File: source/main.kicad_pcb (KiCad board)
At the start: 4 copper layers, 38 x 75 mm, 62 parts, among them J1 pf_533984002, J2 B4B_ZR_SM4_TF, J3 QWIIC, Q1 MOSFET, SW1 _Switch, SW2 _Switch, U1 SCD40, U2 ME6211C33M5G_N, U3 pf_74AHCT2G125, U4 BH1750FVI_TR, U5 ESP32_C3_MINI_1_VIND, U6 TXS0102DCUR, U7 HLK_LD2410B_P, U8 USBLC6_2P6, x1 USB_Type_C_Receptacle_14_pin_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

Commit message: Port layout (wip)
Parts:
- removed C11, C19, C21: 100nF, lcsc:C0402
- removed C20: 1µF, lcsc:C0402
- removed R15, R16: 5.1kΩ, lcsc:R0402
- removed R17: 1MΩ, lcsc:R0402
- removed R3: 1kΩ, lcsc:R0402
- removed SW1, SW2: _Switch, lcsc:KEY-SMD_4P-L4.2-W3.2-P2.20-LS4.6
- added J4: B4B_ZR_SM4_TF, lcsc:CONN-SMD_ZH1.5-4AB, F.Cu at (-34.4, 43.2)
- C1, C13, C14, C16, C5: value 100nF -> 100nF 16V X7R
- C10, C6, C7, C8, C9: value 100nF -> 100nF 16V X7R; moved to F.Cu
- C12: value 1µF -> 100nF 16V X7R; moved to F.Cu
- C15, C3, C4: value 1µF -> 100nF 16V X7R
- C17: value 10µF -> 1µF 25V X5R; footprint lcsc:C0805 -> lcsc:C0402
- C18: value 100nF -> 100nF 1kV X7R; footprint lcsc:C0402 -> lcsc:C2220
- C2: value 4.7µF -> 100nF 16V X7R
- D1: footprint lcsc:LED0805-RD_RED -> lcsc:LED0805-R-RD
- LED1, LED2, LED3, LED4, LED5: moved to F.Cu
- R1, R2, R6, R7, R8, R9: value 10kΩ -> 100Ω
- R10: value 10kΩ -> 100kΩ
- R11: value 100kΩ -> 100Ω
- R12: value 1kΩ -> 5.1kΩ
- R13: value 390Ω -> 5.1kΩ
- R14: value 390Ω -> 1MΩ
- R4, R5: value 10kΩ -> 100Ω; moved to F.Cu
- U3: value pf_74AHCT2G125 -> TXS0102DCUR; footprint lcsc:SC-74A-5_L2.9-W1.6-P0.95-LS2.8-BR -> lcsc:VSON8_L2.0-W2.3-P0.50-LS3.1-BL
- U4: value BH1750FVI_TR -> ESP32_C3_MINI_1; footprint lcsc:WSOF-6_L2.6-W1.6-P0.50-TL-EP -> lcsc:WIFIM-SMD_ESP32-C3-MINI-MINI-1U; moved to F.Cu
- U5: value ESP32_C3_MINI_1_VIND -> TXS0102DCUR; footprint lcsc:WIFIM-SMD_ESP32-C3-MINI-MINI-1U -> lcsc:VSON8_L2.0-W2.3-P0.50-LS3.1-BL
- U6: value TXS0102DCUR -> USBLC6_2P6; footprint lcsc:VSON8_L2.0-W2.3-P0.50-LS3.1-BL -> lcsc:SOT-666-6_L1.6-W1.2-P0.50-LS1.6-BL
- U7: value HLK_LD2410B_P -> BH1750FVI_TR; footprint lcsc:SENSORM-TH_HLK-LD2410B-P -> lcsc:WSOF-6_L2.6-W1.6-P0.50-TL-EP; moved to F.Cu
- U8: value USBLC6_2P6 -> HLK_LD2410B_P; footprint lcsc:SOT-666-6_L1.6-W1.2-P0.50-LS1.6-BL -> lcsc:SENSORM-TH_HLK-LD2410B-P
- moved C18 70.5 mm to (-5.50, 73.0)
- moved LED5 69.5 mm to (-55.7, 52.7)
- moved R13 66.9 mm to (0.50, 68.5), turned to 90 degrees
- moved R14 65.6 mm to (1.50, 68.5), turned to 90 degrees
- moved LED4 63.9 mm to (-55.7, 48.4)
- moved U6 62.2 mm to (-5.00, 64.5), turned to 0 degrees
- moved C3 60.2 mm to (-41.0, 24.9), turned to 0 degrees
- moved C13 59.7 mm to (-34.0, 20.6), turned to 0 degrees
- moved LED3 59.5 mm to (-55.7, 44.1)
- moved U7 56.9 mm to (0.00, 7.00), turned to 180 degrees
- moved LED2 56.7 mm to (-55.7, 39.8)
- moved LED1 55.7 mm to (-55.7, 35.5)
- moved U3 55.5 mm to (-50.8, 53.0), turned to 0 degrees
- moved C4 54.5 mm to (-41.0, 27.0), turned to 0 degrees
- moved R8 54.2 mm to (-27.8, 24.9), turned to 0 degrees
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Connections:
- C12 pad 1: C12-1-R3-1-U4-5 -> 3V3
- C13 pad 1: C13-1-R8-2-SW1-1-SW1-2 -> 3V3
- C14 pad 1: C14-1-R9-2-SW2-1-SW2-2 -> 3V3
- C15 pad 1: C15-1-R10-1-R9-1-U5-8 -> VBUS
- C16 pad 1: 3V3 -> VBUS
- C17 pad 1: 3V3 -> C17-1
- C17 pad 2: GND -> C17-2
- C18 pad 1: 3V3 -> C18-1-R14-1-x1-0
- C2 pad 1: 3V3 -> VBUS
- C3 pad 1: VBUS -> 3V3
- C4 pad 1: 3V3 -> VBUS
- C5 pad 1: C5-1-U3-5 -> VBUS
- C5 pad 2: C5-2-U3-1-U3-3 -> GND
- D1 pad 2: D1-2-R12-2 -> D1-2-R11-1
- J2 pad 1: J2-1-R14-2 -> J2-1
- J2 pad 2: J2-2-R13-2 -> J2-2
- J2 pad 3: VBUS -> J2-3
- J2 pad 4: GND -> J2-4
- LED1 pad 1: LED1-1-U3-4 -> GND
- LED1 pad 2: GND -> LED1-2-U3-8
- LED1 pad 4: LED1-4-LED2-1 -> LED1-4-LED2-2
- LED2 pad 1: LED1-4-LED2-1 -> GND
- LED2 pad 2: GND -> LED1-4-LED2-2
- LED2 pad 4: LED2-4-LED3-1 -> LED2-4-LED3-2
- LED3 pad 1: LED2-4-LED3-1 -> GND
- LED3 pad 2: GND -> LED2-4-LED3-2
- LED3 pad 4: LED3-4-LED4-1 -> LED3-4-LED4-2
- LED4 pad 1: LED3-4-LED4-1 -> GND
- LED4 pad 2: GND -> LED3-4-LED4-2
- LED4 pad 4: LED4-4-LED5-1 -> LED4-4-LED5-2
- LED5 pad 1: LED4-4-LED5-1 -> GND
- LED5 pad 2: GND -> LED4-4-LED5-2
- Q1 pad 1: Q1-1-R11-1-U5-21 -> Q1-1-R9-1-U4-21
- R1 pad 1: SDA -> SCL
- R10 pad 1: C15-1-R10-1-R9-1-U5-8 -> R10-1
- R10 pad 2: 3V3 -> R10-2
- R11 pad 1: Q1-1-R11-1-U5-21 -> D1-2-R11-1
- R11 pad 2: GND -> R11-2
- R12 pad 1: R12-1 -> R12-1-x1-12
- R12 pad 2: D1-2-R12-2 -> GND
- R13 pad 1: U1_RX_BHV -> R13-1-x1-5
- R13 pad 2: J2-2-R13-2 -> GND
- R14 pad 1: U1_TX_BHV -> C18-1-R14-1-x1-0
- R14 pad 2: J2-1-R14-2 -> GND
- R2 pad 1: SCL -> SDA
- R4 pad 1: SDA -> SCL
- R5 pad 1: SCL -> SDA
- R6 pad 1: R6-1-U5-22 -> R6-1-U4-8
- R6 pad 2: 3V3 -> R6-2
- R7 pad 1: R7-1-U5-5 -> R7-1-U4-5
- R7 pad 2: 3V3 -> R7-2
- R8 pad 1: R8-1-U5-23 -> R8-1-U4-22
- R8 pad 2: C13-1-R8-2-SW1-1-SW1-2 -> R8-2
- R9 pad 1: C15-1-R10-1-R9-1-U5-8 -> Q1-1-R9-1-U4-21
- R9 pad 2: C14-1-R9-2-SW2-1-SW2-2 -> R9-2
- U3 pad 1: C5-2-U3-1-U3-3 -> U3-1
- U3 pad 2: U3-2 -> GND
- U3 pad 3: C5-2-U3-1-U3-3 -> VBUS
- U3 pad 4: LED1-1-U3-4 -> U3-4
- U3 pad 5: C5-1-U3-5 -> U3-5
- U4 pad 1: 3V3 -> GND
- U4 pad 2: U4-2 -> GND
- U4 pad 3: GND -> 3V3
- U4 pad 4: SDA -> U4-4
- U4 pad 5: C12-1-R3-1-U4-5 -> R7-1-U4-5
- U4 pad 6: SCL -> U4-6
- U5 pad 1: GND -> U5-1
- U5 pad 5: R7-1-U5-5 -> U5-5
- U5 pad 6: U5-6 -> 3V3
- U5 pad 7: U5-7 -> VBUS
- U5 pad 8: C15-1-R10-1-R9-1-U5-8 -> U5-8
- U6 pad 1: U1_RX_BHV -> USB_DP
- U6 pad 3: 3V3 -> USB_DN
- U6 pad 4: U1_RX -> USB_DN
- U6 pad 5: U1_TX -> VBUS
- U6 pad 6: GND -> USB_DP
- U7 pad 1: U5-20-U7-1 -> 3V3
- U7 pad 2: U0_TX -> U7-2
- U7 pad 3: U0_RX -> GND
- U7 pad 4: GND -> SDA
- U7 pad 5: VBUS -> U7-5
- U8 pad 1: USB_DP -> U4-20-U8-1
- U8 pad 2: GND -> DSF_MCU_UART0_TX
- U8 pad 3: USB_DN -> DSF_MCU_UART0_RX
- U8 pad 4: USB_DN -> GND
- x1 pad 0: C21-1-R17-1-x1-0 -> C18-1-R14-1-x1-0
- x1 pad 12: R15-1-x1-12 -> R12-1-x1-12
- x1 pad 5: R16-1-x1-5 -> R13-1-x1-5
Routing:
- net (no net): track 0.00 -> 70.6 mm, vias 0 -> 2
- net LED1-1-U3-4: track 12.0 -> 0.00 mm, vias 1 -> 0
- net LED4-4-LED5-1: track 8.46 -> 0.00 mm
- net LED2-4-LED3-1: track 8.46 -> 0.00 mm
- net LED1-4-LED2-1: track 8.46 -> 0.00 mm
- net LED3-4-LED4-1: track 8.46 -> 0.00 mm
- net C21-1-R17-1-x1-0: track 8.03 -> 0.00 mm
- net C17-2: track 0.00 -> 7.58 mm
- net C14-1-R9-2-SW2-1-SW2-2: track 7.58 -> 0.00 mm
- net C13-1-R8-2-SW1-1-SW1-2: track 7.58 -> 0.00 mm
- net R16-1-x1-5: track 6.74 -> 0.00 mm
- net R15-1-x1-12: track 5.63 -> 0.00 mm
- net R12-1-x1-12: track 0.00 -> 5.63 mm
- net R6-1-U4-8: track 0.00 -> 4.67 mm
- net C15-1-R10-1-R9-1-U5-8: track 4.67 -> 0.00 mm
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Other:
- outline, holes or cut-outs redrawn

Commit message: Various fixes and changes
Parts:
- removed R11, R6: 100Ω, lcsc:R0402
- removed R12, R13: 5.1kΩ, lcsc:R0402
- removed R14: 1MΩ, lcsc:R0402
- removed x1: USB_Type_C_Receptacle_14_pin_Vertical, lcsc:USB-C-TH_TYPE-C-USB-14P
- added C11: 1µF 25V X5R, lcsc:C0402, B.Cu at (1.50, 32.3)
- added C19: 1µF 25V X5R, lcsc:C0402, F.Cu at (-6.00, 61.5)
- added C20: 100nF 16V X7R, lcsc:C0402, F.Cu at (-2.50, 68.5)
- added D2: LED, lcsc:LED0805-R-RD, F.Cu at (8.00, 30.0)
- added F1: Fuse, lcsc:F0603, F.Cu at (15.0, 7.50)
- added F2: Fuse, lcsc:F0402, F.Cu at (2.75, 68.5)
- added R3: 100Ω, lcsc:R0402, B.Cu at (3.00, 6.00)
- added S1: Button, lcsc:KEY-SMD_4P-L4.2-W3.2-P2.20-LS4.6, F.Cu at (13.5, 61.5)
- added S2: Button, lcsc:KEY-SMD_4P-L4.2-W3.2-P2.20-LS4.6, F.Cu at (-13.5, 61.5)
- added U9: USB2_0_ESD_Protection, lcsc:SOT-666-6_L1.6-W1.2-P0.50-LS1.6-BL, F.Cu at (-8.00, 61.5)
- C1, C14, C15, C16, C2, C3, C4, C5, C6, C7: value 100nF 16V X7R -> 1µF 25V X5R
- C10, C12, C8, C9: value 100nF 16V X7R -> 1µF 25V X5R; moved to B.Cu
- C13, LED1, LED2, LED3, LED4, LED5, R4, U8: moved to B.Cu
- C18: value 100nF 1kV X7R -> 1µF 25V X5R; footprint lcsc:C2220 -> lcsc:C0402
- D1: value LED -> 1.1V; footprint lcsc:LED0805-R-RD -> lcsc:SOD-123F_L2.8-W1.8-LS3.7-RD
- H1, H2, H3: footprint MountingHole:MountingHole_2.1mm -> MountingHole:MountingHole_2mm
- J4: value B4B_ZR_SM4_TF -> USB_Type_C_Receptacle_14_pin_Vertical; footprint lcsc:CONN-SMD_ZH1.5-4AB -> lcsc:USB-C-TH_TYPE-C-USB-14P
- R10: value 100kΩ -> 1MΩ
- R8, R9: value 100Ω -> 5.1kΩ
- U3: value TXS0102DCUR -> ME6211C33M5G_N; footprint lcsc:VSON8_L2.0-W2.3-P0.50-LS3.1-BL -> lcsc:SOT-23-5_L3.0-W1.7-P0.95-LS2.8-BL
- U4: value ESP32_C3_MINI_1 -> TXS0102DCUR; footprint lcsc:WIFIM-SMD_ESP32-C3-MINI-MINI-1U -> lcsc:VSON8_L2.0-W2.3-P0.50-LS3.1-BL
- U5: value TXS0102DCUR -> BH1750FVI_TR; footprint lcsc:VSON8_L2.0-W2.3-P0.50-LS3.1-BL -> lcsc:WSOF-6_L2.6-W1.6-P0.50-TL-EP; moved to B.Cu
- U6: value USBLC6_2P6 -> ESP32_C3_MINI_1; footprint lcsc:SOT-666-6_L1.6-W1.2-P0.50-LS1.6-BL -> lcsc:WIFIM-SMD_ESP32-C3-MINI-MINI-1U
- U7: value BH1750FVI_TR -> TXS0102DCUR; footprint lcsc:WSOF-6_L2.6-W1.6-P0.50-TL-EP -> lcsc:VSON8_L2.0-W2.3-P0.50-LS3.1-BL
- moved C18 70.8 mm to (-3.00, 2.20)
- moved C17 62.6 mm to (3.25, 2.80), turned to -90 degrees
- moved LED1 60.8 mm to (0.00, 11.0), turned to 180 degrees
- moved LED2 60.1 mm to (0.00, 17.1), turned to 180 degrees
- moved LED3 59.5 mm to (0.00, 23.2), turned to 180 degrees
- moved LED4 58.9 mm to (0.00, 29.3), turned to 180 degrees
- moved LED5 58.3 mm to (0.00, 35.4), turned to 180 degrees
- moved C5 57.1 mm to (3.85, 64.5), turned to -90 degrees
- moved C4 56.5 mm to (5.60, 59.0), turned to 180 degrees
- moved U3 56.4 mm to (5.00, 61.5), turned to 90 degrees
- moved C3 55.5 mm to (-2.15, 64.5), turned to -90 degrees
- moved C2 54.5 mm to (-0.40, 59.0), turned to 180 degrees
- moved U6 51.8 mm to (-11.0, 13.0), turned to 90 degrees
- moved R8 51.0 mm to (-1.25, 68.5), turned to 90 degrees
- moved R9 49.9 mm to (0.00, 68.5), turned to 90 degrees
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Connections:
- net U7-5 renamed DSF_MCU_UART1_RX
- C1 pad 1: 3V3 -> 3V3_PERIPHERAL
- C10 pad 1: VBUS -> 5V
- C12 pad 1: 3V3 -> 5V
- C13 pad 1: 3V3 -> 3V3_PERIPHERAL
- C14 pad 1: 3V3 -> 3V3_MCU
- C15 pad 1: VBUS -> MCU_GPIO0
- C16 pad 1: VBUS -> MCU_GPIO1
- C17 pad 1: C17-1 -> 3V3_PERIPHERAL
- C17 pad 2: C17-2 -> GND
- C18 pad 1: C18-1-R14-1-x1-0 -> 5V
- C2 pad 1: VBUS -> 5V
- C3 pad 1: 3V3 -> 3V3_MCU
- C4 pad 1: VBUS -> 5V
- C5 pad 1: VBUS -> 3V3_PERIPHERAL
- C6 pad 1: VBUS -> 3V3_PERIPHERAL
- C7 pad 1: VBUS -> 5V
- C8 pad 1: VBUS -> 5V
- C9 pad 1: VBUS -> 5V
- D1 pad 1: VBUS -> D1-1-J1-1-Q1-2-R7-2
- D1 pad 2: D1-2-R11-1 -> 5V
- J1 pad 1: J1-1-Q1-2 -> D1-1-J1-1-Q1-2-R7-2
- J1 pad 2: VBUS -> 5V
- J2 pad 1: J2-1 -> USF_PM_SENSOR_LEVEL_SHIFTER_RX
- J2 pad 2: J2-2 -> USF_PM_SENSOR_LEVEL_SHIFTER_TX
- J2 pad 3: J2-3 -> 5V
- J2 pad 4: J2-4 -> GND
- J3 pad 2: 3V3 -> F1-1-J3-2
- J4 pad 1: DFS_MCU_UART1_RX -> GND
- J4 pad 2: DFS_MCU_UART1_TX -> VBUS
- J4 pad 3: J4-3 -> USB_DN
- J4 pad 4: J4-4 -> USB_DP
- J4 pad 5: J4-5 -> J4-5-R9-1
- J4 pad 6: J4-6 -> VBUS
- LED1 pad 2: LED1-2-U3-8 -> LED1-2-U4-8
- LED1 pad 3: VBUS -> 5V
- LED2 pad 3: VBUS -> 5V
- LED3 pad 3: VBUS -> 5V
- LED4 pad 3: VBUS -> 5V
- LED5 pad 3: VBUS -> 5V
- Q1 pad 1: Q1-1-R9-1-U4-21 -> MCU_GPIO7
- Q1 pad 2: J1-1-Q1-2 -> D1-1-J1-1-Q1-2-R7-2
- R1 pad 2: 3V3 -> 3V3_PERIPHERAL
- R10 pad 1: R10-1 -> C20-1-J4-0-R10-1
- R10 pad 2: R10-2 -> GND
- R2 pad 2: 3V3 -> 3V3_PERIPHERAL
- R4 pad 1: SCL -> SDA
- R4 pad 2: 3V3 -> 3V3_PERIPHERAL
- R5 pad 1: SDA -> MCU_GPIO7
- R5 pad 2: 3V3 -> GND
- R7 pad 1: R7-1-U4-5 -> D2-2-R7-1
- R7 pad 2: R7-2 -> D1-1-J1-1-Q1-2-R7-2
- R8 pad 1: R8-1-U4-22 -> J4-12-R8-1
- R8 pad 2: R8-2 -> GND
- R9 pad 1: Q1-1-R9-1-U4-21 -> J4-5-R9-1
- R9 pad 2: R9-2 -> GND
- U1 pad 19: 3V3 -> 3V3_PERIPHERAL
- U1 pad 7: 3V3 -> 3V3_PERIPHERAL
- U2 pad 1: VBUS -> 5V
- U2 pad 3: VBUS -> 5V
- U2 pad 5: 3V3 -> 3V3_MCU
- U3 pad 1: U3-1 -> 5V
- U3 pad 3: VBUS -> 5V
- U3 pad 5: U3-5 -> 3V3_PERIPHERAL
- U4 pad 1: GND -> U4-1
- U4 pad 3: 3V3 -> 3V3_PERIPHERAL
- U4 pad 5: R7-1-U4-5 -> MCU_GPIO5
- U4 pad 6: U4-6 -> 3V3_PERIPHERAL
- U4 pad 7: U4-7 -> 5V
- U4 pad 8: R6-1-U4-8 -> LED1-2-U4-8
- U5 pad 1: U5-1 -> 3V3_PERIPHERAL
- U5 pad 2: GND -> U5-2
- U5 pad 3: 3V3 -> GND
- U5 pad 4: U5-4 -> SDA
- U5 pad 6: 3V3 -> SCL
- U5 pad 7: VBUS -> U5-7
- U6 pad 1: USB_DP -> GND
- U6 pad 3: USB_DN -> 3V3_MCU
- U6 pad 4: USB_DN -> U6-4
- U6 pad 5: VBUS -> MCU_GPIO2
- U6 pad 6: USB_DP -> MCU_GPIO3
- U7 pad 1: 3V3 -> USF_PM_SENSOR_LEVEL_SHIFTER_TX
- U7 pad 2: U7-2 -> GND
- U7 pad 3: GND -> 3V3_PERIPHERAL
- U7 pad 4: SDA -> DSF_MCU_UART1_TX
- U7 pad 6: SCL -> 3V3_PERIPHERAL
- U7 pad 7: U7-7 -> 5V
- U8 pad 1: U4-20-U8-1 -> MCU_GPIO6
- U8 pad 5: VBUS -> 5V
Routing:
- net (no net): track 70.6 -> 0.00 mm, vias 2 -> 0
- net VBUS: track 56.0 -> 17.6 mm, vias 5 -> 1
- net 3V3: track 32.9 -> 0.00 mm, vias 1 -> 0
- net USB_DP: track 72.7 -> 54.6 mm, vias 3 -> 1
- net USB_DN: track 72.7 -> 54.7 mm, vias 3 -> 1
- net SDA: track 0.00 -> 17.4 mm, vias 0 -> 2
- net SCL: track 0.00 -> 16.1 mm, vias 0 -> 2
- net 5V: track 0.00 -> 12.9 mm, vias 0 -> 4
- net 3V3_PERIPHERAL: track 0.00 -> 12.8 mm
- net D1-1-J1-1-Q1-2-R7-2: track 0.00 -> 12.8 mm
- net F1-1-J3-2: track 0.00 -> 8.05 mm, vias 0 -> 2
- net C17-2: track 7.58 -> 0.00 mm
- net R12-1-x1-12: track 5.63 -> 0.00 mm
- net J4-5-R9-1: track 0.00 -> 5.53 mm
- net C20-1-J4-0-R10-1: track 0.00 -> 5.08 mm
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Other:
- outline, holes or cut-outs redrawn
- board text added: "80082e6"
- board text added: "Vindriktning"

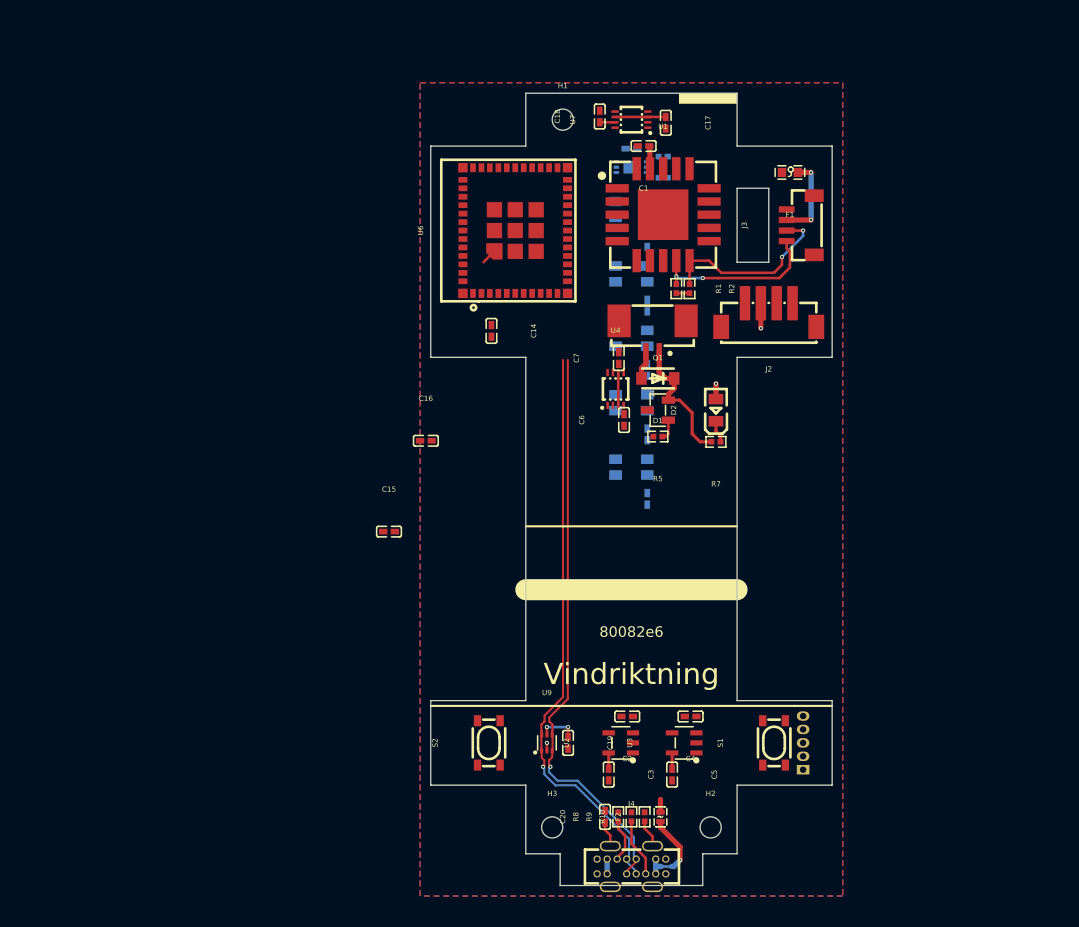
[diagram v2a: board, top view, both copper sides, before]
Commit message: fix power source short
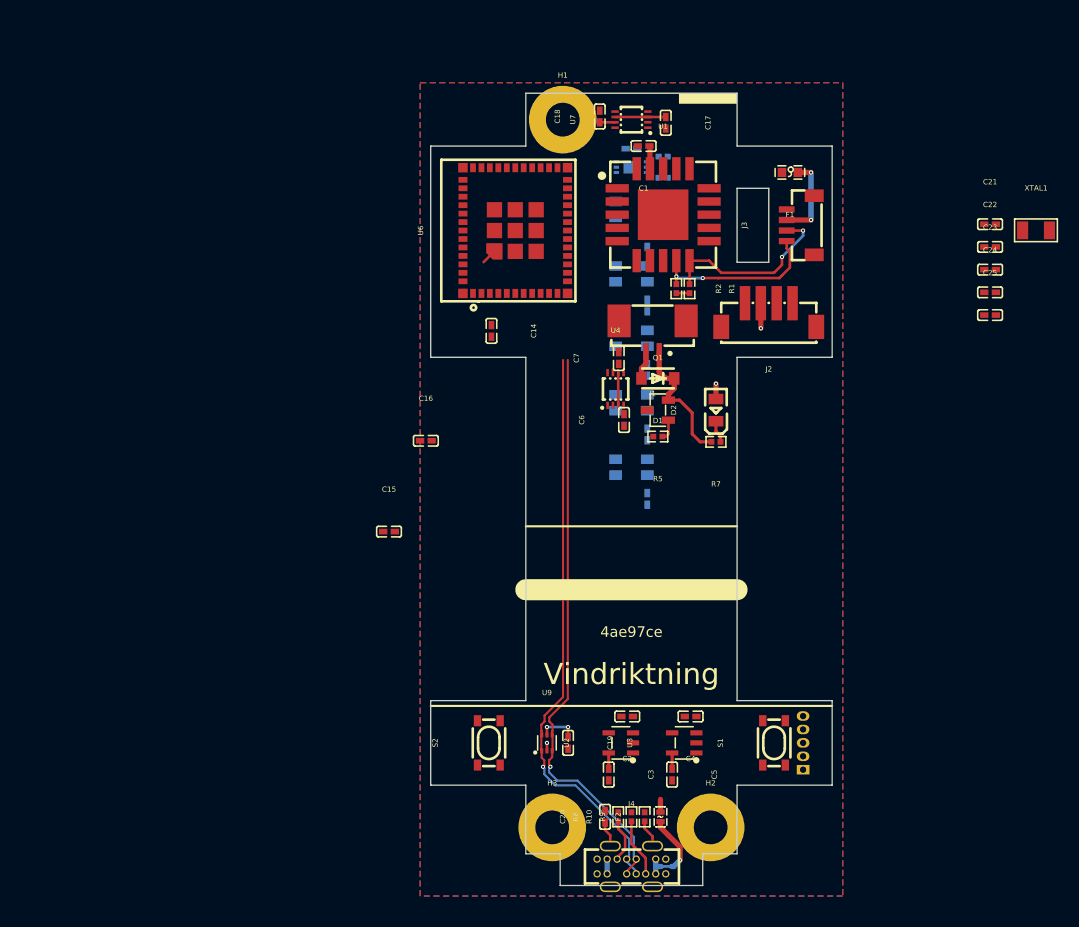
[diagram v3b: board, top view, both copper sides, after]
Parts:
- added C21: 100nF 16V X7R, lcsc:C0402, F.Cu at (34.0, 12.4)
- added C22: 100nF 16V X7R, lcsc:C0402, F.Cu at (34.0, 14.6)
- added C23: 100nF 16V X7R, lcsc:C0402, F.Cu at (34.0, 16.7)
- added C24: 100nF 16V X7R, lcsc:C0402, F.Cu at (34.0, 18.9)
- added C25: 100nF 16V X7R, lcsc:C0402, F.Cu at (34.0, 21.0)
- added XTAL1: Crystal, lcsc:CRYSTAL-SMD_L3.2-W1.5-1, F.Cu at (38.3, 13.0)
- C1, C10, C11, C12, C14, C17, C18, C19, C2, C3, C4, C5, C6, C7, C8, C9: value 1µF 25V X5R -> 100nF 16V X7R
- C15, C16: value 1µF 25V X5R -> 15pF 50V C0G
- D2: value LED -> 2V
- H1, H2, H3: footprint MountingHole:MountingHole_2mm -> MountingHole:MountingHole_3.2mm_M3_Pad
- R7: value 100Ω -> 2.2kΩ
- U2: value ME6211C33M5G_N -> LDO 3.3V ±2% Vin max 4.8V - 5.2V Iq
- U3: value ME6211C33M5G_N -> LDO 3.3V Vin max 4.8V - 5.2V Iq
- moved LED3 12.2 mm to (0.00, 11.0)
- moved LED5 12.2 mm to (0.00, 23.2)
- moved LED2 12.2 mm to (0.00, 29.3)
- moved LED1 6.10 mm to (0.00, 17.1)
- moved LED4 6.10 mm to (0.00, 35.4)
- moved R1 1.25 mm to (5.50, 18.5)
- moved R10 1.25 mm to (0.00, 68.5)
- moved R2 1.25 mm to (4.25, 18.5)
- moved R9 1.25 mm to (1.25, 68.5)
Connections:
- C6 pad 1: 3V3_PERIPHERAL -> 5V
- R1 pad 2: 3V3_PERIPHERAL -> R1-2-R2-2
- R2 pad 2: 3V3_PERIPHERAL -> R1-2-R2-2
- S1 pad 1: S1-1-S1-2 -> S1-1-S1-2-U6-8
- S1 pad 2: S1-1-S1-2 -> S1-1-S1-2-U6-8
- S1 pad 3: S1-3-S1-4 -> GND
- S1 pad 4: S1-3-S1-4 -> GND
- S2 pad 1: S2-1-S2-2 -> MCU_GPIO9
- S2 pad 2: S2-1-S2-2 -> MCU_GPIO9
- S2 pad 3: S2-3-S2-4 -> GND
- S2 pad 4: S2-3-S2-4 -> GND
- U2 pad 3: 5V -> U2-3-U3-3
- U3 pad 3: 5V -> U2-3-U3-3
- U6 pad 8: U6-8 -> S1-1-S1-2-U6-8
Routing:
- net R1-2-R2-2: track 0.00 -> 1.25 mm
- net 3V3_PERIPHERAL: track 12.8 -> 11.6 mm
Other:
- board text added: "4ae97ce"
- board text removed: "80082e6"

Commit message: Fix some layout
- Add named net for fan
- Add part db to gitignore
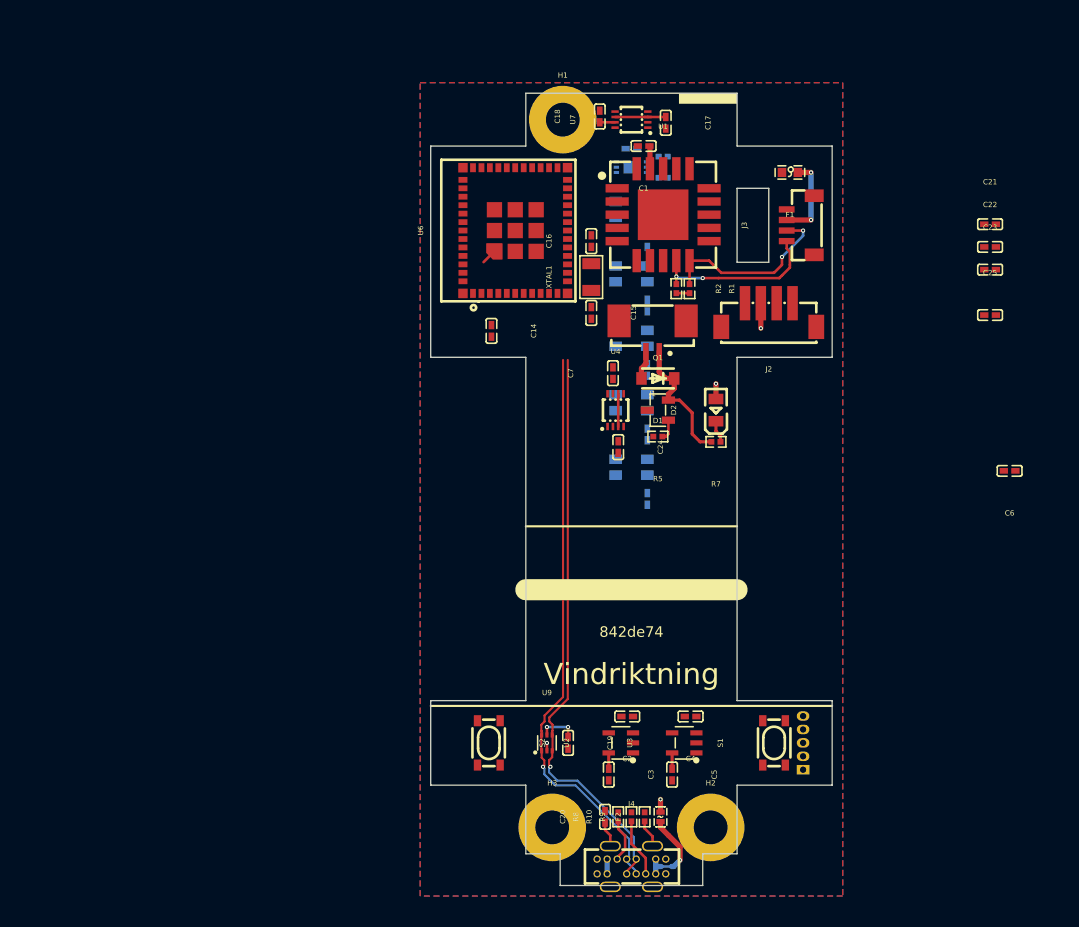
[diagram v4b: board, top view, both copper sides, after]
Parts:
- moved XTAL1 42.3 mm to (-3.80, 17.4), turned to 90 degrees
- moved C24 38.1 mm to (-1.25, 33.5), turned to -90 degrees
- moved C6 36.8 mm to (35.8, 35.8), turned to 180 degrees
- moved C15 28.2 mm to (-3.80, 20.8), turned to -90 degrees
- moved C16 24.5 mm to (-3.80, 14.0), turned to 90 degrees
- moved LED3 18.3 mm to (0.00, 29.3)
- moved LED4 18.3 mm to (0.00, 17.1)
- moved LED5 12.2 mm to (0.00, 35.4)
- moved LED1 6.10 mm to (0.00, 11.0)
- moved LED2 6.10 mm to (0.00, 23.2)
- moved R3 2.00 mm to (3.00, 8.00)
- moved R4 2.00 mm to (3.00, 6.00)
- moved U4 2.00 mm to (-1.50, 30.0)
- moved C7 1.53 mm to (-1.75, 26.5)
- turned S2 to -90 degrees
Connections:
- net D1-1-J1-1-Q1-2-R7-2 renamed FAN_OUT-
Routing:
- net 5V: vias 4 -> 5
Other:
- board text added: "842de74"
- board text removed: "4ae97ce"
